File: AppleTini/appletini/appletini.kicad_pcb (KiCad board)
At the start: 2 copper layers, 114.3 x 69.8 mm, 28 parts, among them J1 Conn_02x25_Counter_Clockwise, Q1 DMG2305UX-7, U1 74LS245, U10 74LS07, U16 Pico, U17 Teensy4.1, U2 74LS245, U3 74LS245, U4 74LS245, U9 74LS245

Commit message: part picks and cleanup
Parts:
- R9: value 10k -> 10K

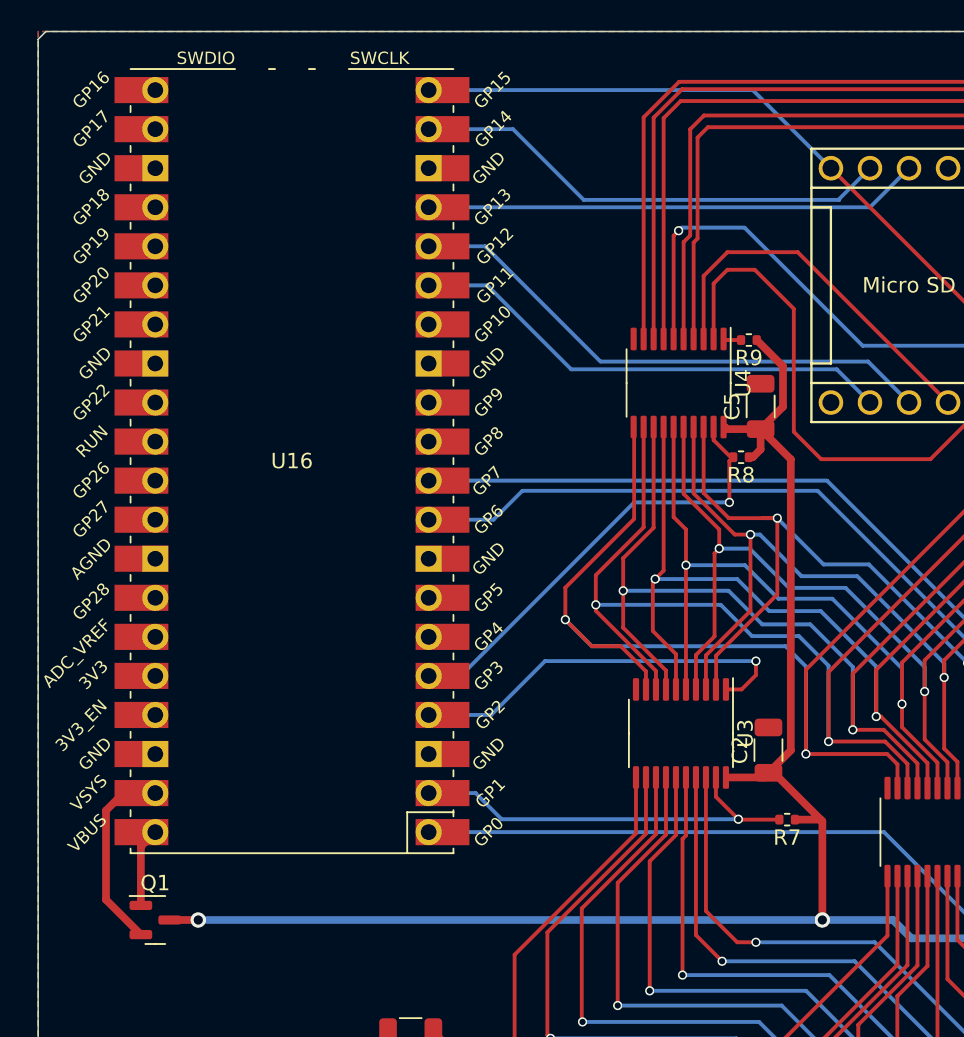
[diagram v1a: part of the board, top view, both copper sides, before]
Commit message: Add pico reset, rotate pico to point USB up
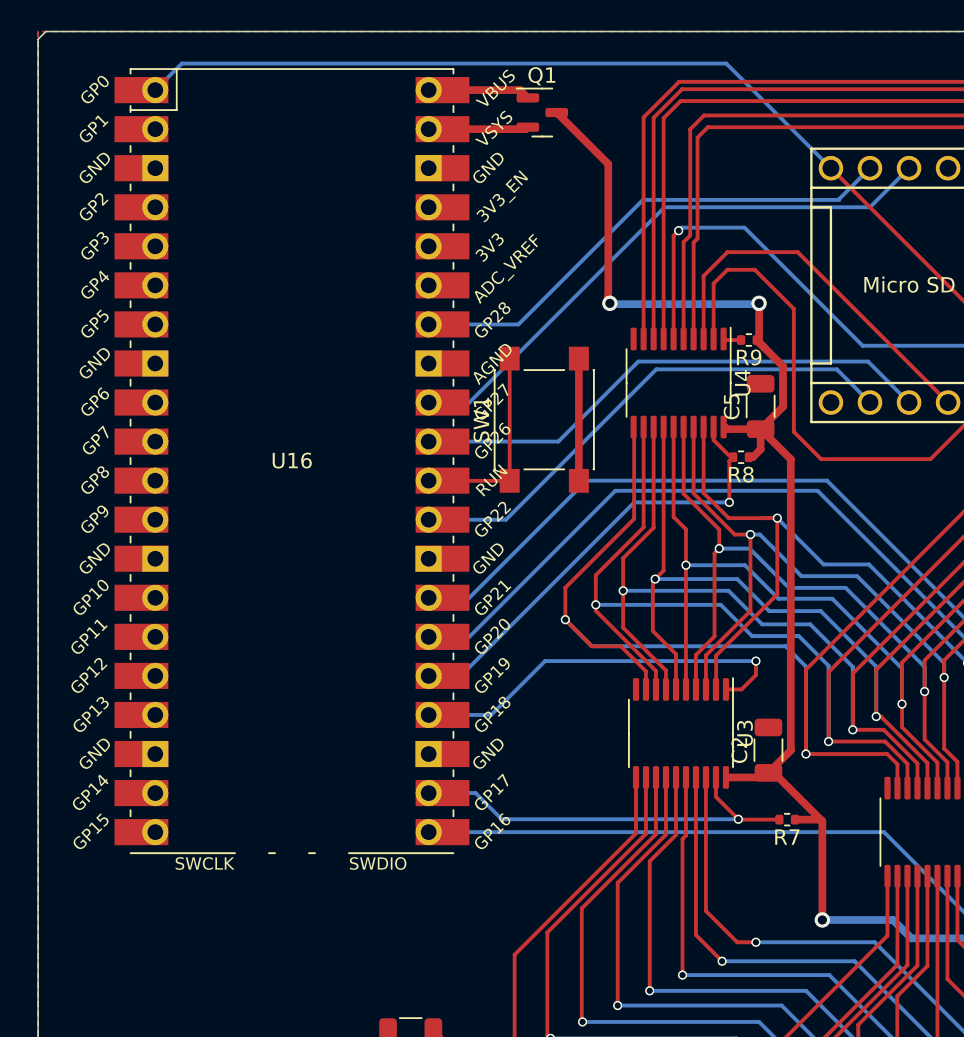
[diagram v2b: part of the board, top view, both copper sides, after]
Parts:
- added SW1: SW_Push, Button_Switch_SMD:SW_Push_1P1T_NO_6x6mm_H9.5mm, F.Cu at (109.1, 88.7)
- moved Q1 58.2 mm to (109.0, 68.8)
- turned U16 to 0 degrees
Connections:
- U16 pad 1: /ALO_EN -> /PHI0
- U16 pad 10: /RDY -> unconnected-(U16-GPIO7-Pad10)
- U16 pad 15: /INH_REQ -> unconnected-(U16-GPIO11-Pad15)
- U16 pad 16: /RDY_REQ -> unconnected-(U16-GPIO12-Pad16)
- U16 pad 17: /TEENSY_IRQ -> unconnected-(U16-GPIO13-Pad17)
- U16 pad 19: /OUT_D_REQ -> unconnected-(U16-GPIO14-Pad19)
- U16 pad 2: /D_EN -> unconnected-(U16-GPIO1-Pad2)
- U16 pad 20: /PHI0 -> unconnected-(U16-GPIO15-Pad20)
- U16 pad 21: unconnected-(U16-GPIO16-Pad21) -> /ALO_EN
- U16 pad 22: unconnected-(U16-GPIO17-Pad22) -> /D_EN
- U16 pad 24: unconnected-(U16-GPIO18-Pad24) -> /D_DIR
- U16 pad 25: unconnected-(U16-GPIO19-Pad25) -> /OUT_D_EN
- U16 pad 26: unconnected-(U16-GPIO20-Pad26) -> /INH
- U16 pad 27: unconnected-(U16-GPIO21-Pad27) -> /RDY
- U16 pad 29: unconnected-(U16-GPIO22-Pad29) -> /INH_REQ
- U16 pad 30: unconnected-(U16-RUN-Pad30) -> Net-(U16-RUN)
- U16 pad 31: unconnected-(U16-GPIO26_ADC0-Pad31) -> /RDY_REQ
- U16 pad 32: unconnected-(U16-GPIO27_ADC1-Pad32) -> /TEENSY_IRQ
- U16 pad 34: unconnected-(U16-GPIO28_ADC2-Pad34) -> /OUT_D_REQ
- U16 pad 4: /D_DIR -> unconnected-(U16-GPIO2-Pad4)
- U16 pad 5: /OUT_D_EN -> unconnected-(U16-GPIO3-Pad5)
- U16 pad 9: /INH -> unconnected-(U16-GPIO6-Pad9)
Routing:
- net /PHI0: track 85.9 -> 105.1 mm
- net +3.3V: track 232.1 -> 216.7 mm, vias 10 -> 11
- net Net-(U16-RUN): track 0.00 -> 13.2 mm
- net GND: track 68.7 -> 76.7 mm
- net /VSYS: track 14.4 -> 6.51 mm
- net /TEENSY_IRQ: track 32.3 -> 37.6 mm
- net unconnected-(U16-GPIO14-Pad19): track 0.00 -> 3.74 mm
- net /RDY: track 94.9 -> 98.0 mm
- net /INH: track 78.7 -> 81.9 mm
- net /INH_REQ: track 31.9 -> 33.6 mm
- net /VBUS: track 5.15 -> 6.66 mm
- net /OUT_D_REQ: track 31.5 -> 32.9 mm
- net /RDY_REQ: track 35.5 -> 34.5 mm

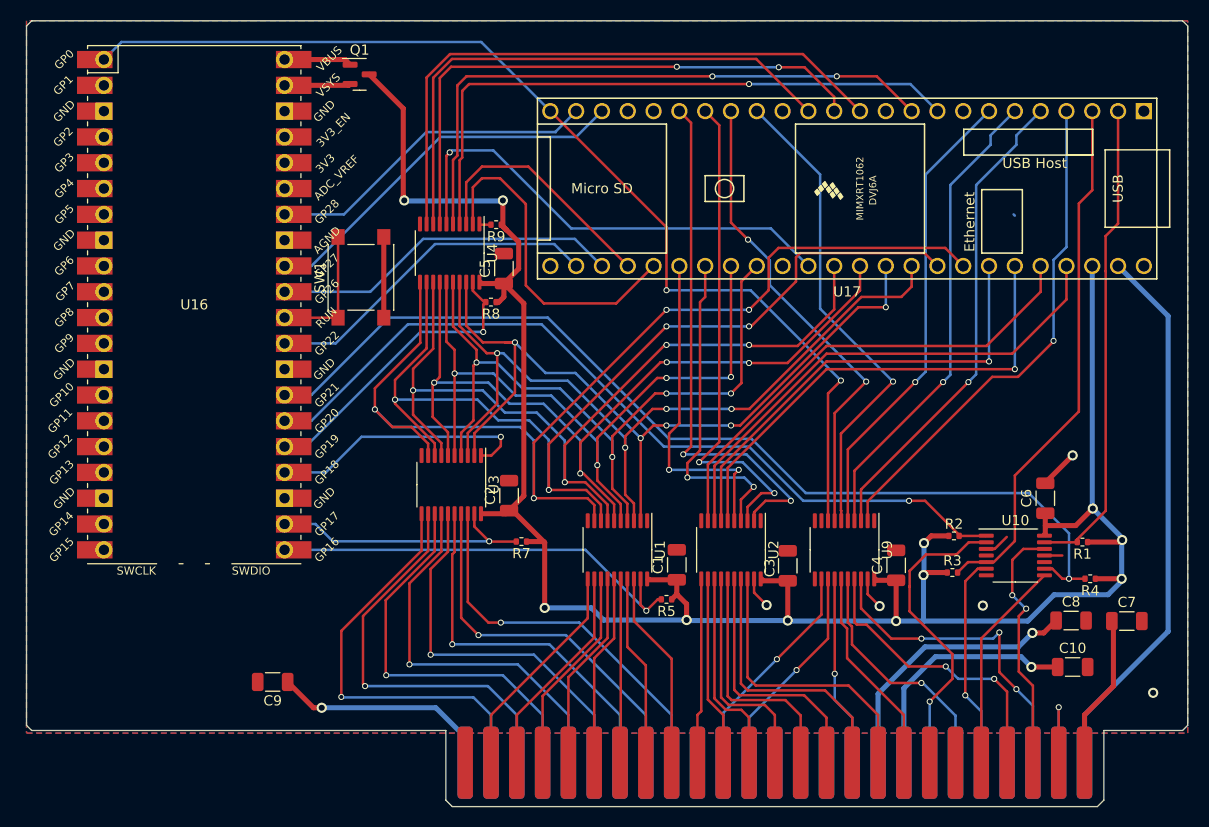
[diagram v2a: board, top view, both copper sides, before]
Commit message: reduce board to 2.625in vertical
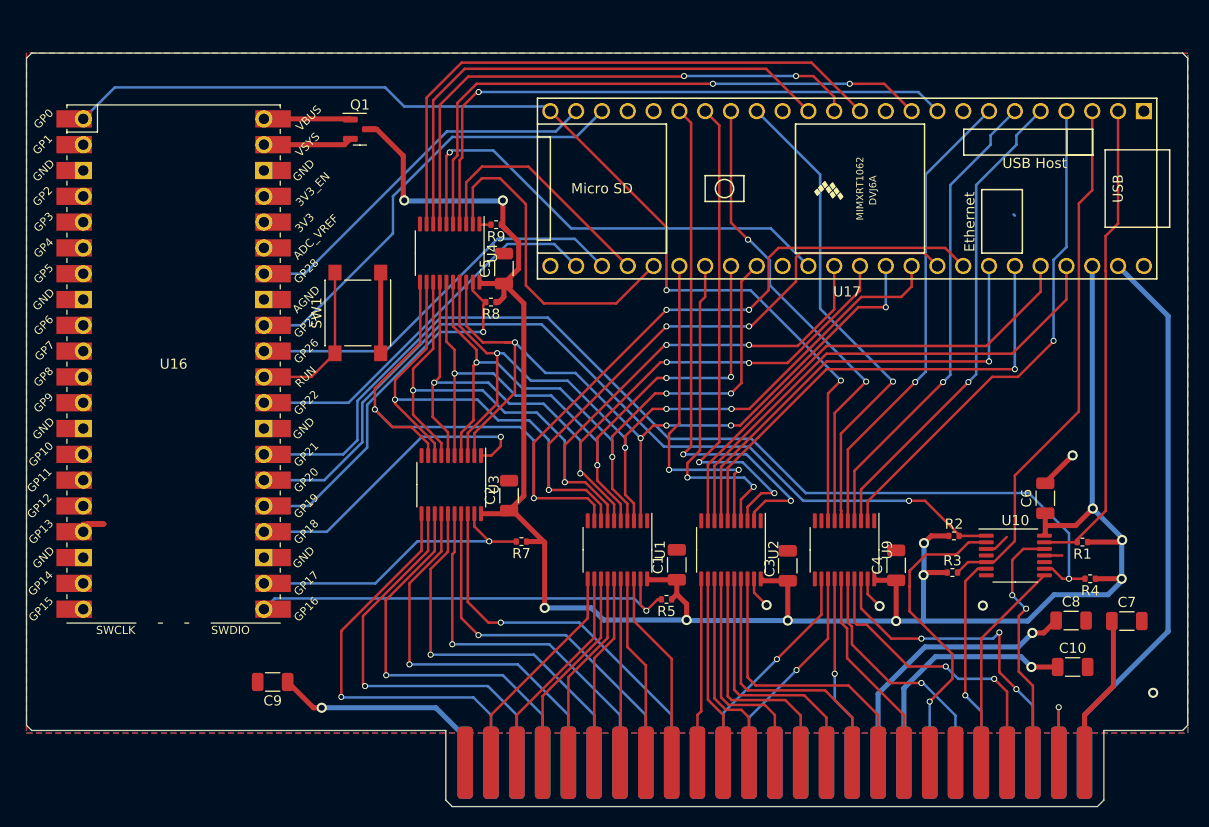
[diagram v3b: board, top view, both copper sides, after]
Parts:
- moved U16 6.19 mm to (90.7, 97.3)
- moved Q1 5.40 mm to (109.0, 74.2)
- moved SW1 3.52 mm to (108.8, 92.3)
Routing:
- net /OUT_D_EN: track 29.9 -> 36.8 mm
- net /RDY: track 98.0 -> 104.8 mm
- net /INH: track 81.9 -> 88.6 mm
- net /TEENSY_IRQ: track 37.6 -> 44.2 mm
- net +3.3V: track 216.7 -> 211.7 mm
- net /D_DIR: track 26.0 -> 30.4 mm
- net /RDY_REQ: track 34.5 -> 39.0 mm
- net /INH_REQ: track 33.6 -> 38.1 mm
- net /OUT_D_REQ: track 32.9 -> 37.4 mm
- net unconnected-(U16-GPIO14-Pad19): track 3.74 -> 0.00 mm
- net unconnected-(U16-GPIO13-Pad17): track 0.00 -> 3.74 mm
- net /D_EN: track 26.8 -> 29.9 mm
- net Net-(U16-RUN): track 13.2 -> 15.9 mm
- net /Transceivers/OUT_D2: track 56.3 -> 54.0 mm
- net /VSYS: track 6.51 -> 8.75 mm
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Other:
- board size 114.3 x 69.8 mm -> 114.3 x 66.7 mm

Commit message: traces wiped
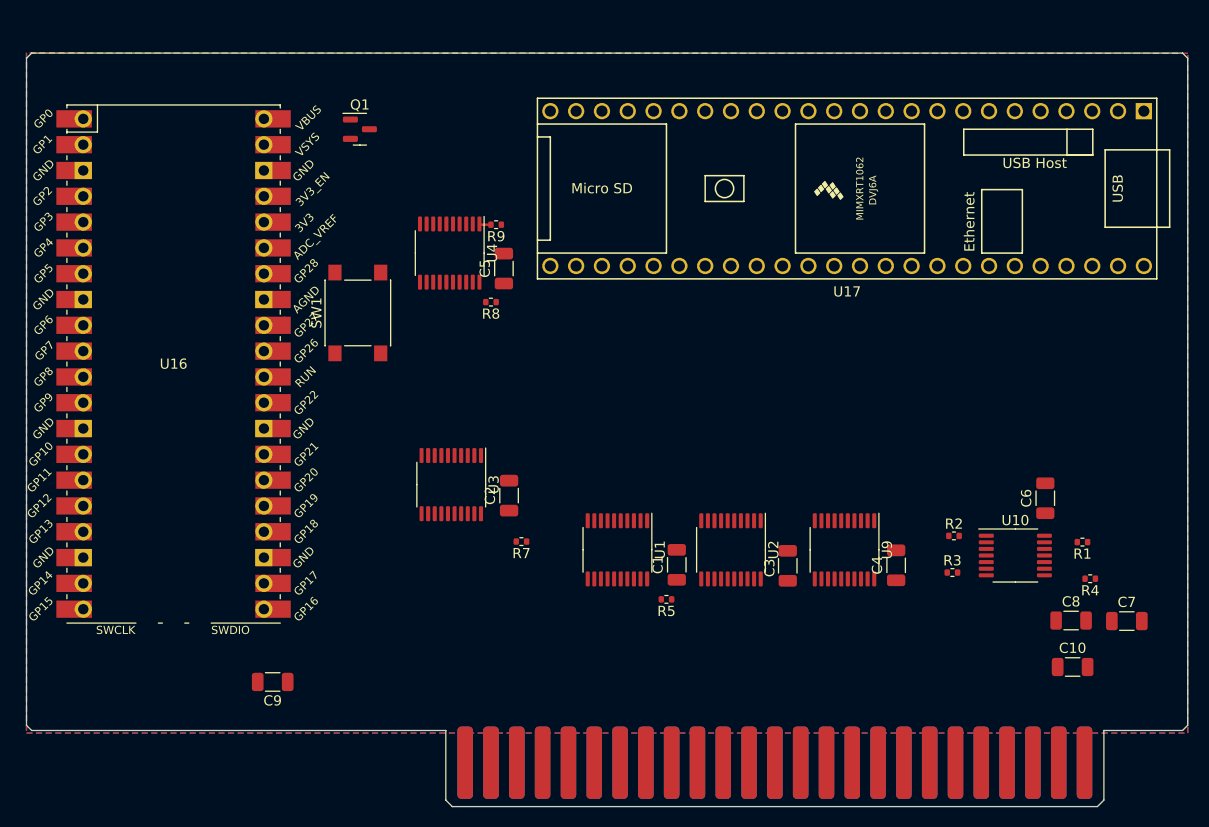
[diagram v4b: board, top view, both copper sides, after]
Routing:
- net +3.3V: track 211.7 -> 0.00 mm, vias 11 -> 0
- net /Transceivers/ALO_D0: track 110.9 -> 0.00 mm, vias 4 -> 0
- net /PHI0: track 105.8 -> 0.00 mm, vias 2 -> 0
- net /RDY: track 104.8 -> 0.00 mm, vias 1 -> 0
- net /Transceivers/ALO_D1: track 101.5 -> 0.00 mm, vias 4 -> 0
- net /INH: track 88.6 -> 0.00 mm, vias 1 -> 0
- net /Transceivers/ALO_D2: track 86.9 -> 0.00 mm, vias 4 -> 0
- net /Transceivers/ALO_D3: track 83.4 -> 0.00 mm, vias 4 -> 0
- net /Transceivers/ALO_D6: track 82.4 -> 0.00 mm, vias 4 -> 0
- net /Transceivers/ALO_D7: track 81.5 -> 0.00 mm, vias 5 -> 0
- net GND: track 76.7 -> 0.00 mm, vias 5 -> 0
- net /Transceivers/ALO_D5: track 72.8 -> 0.00 mm, vias 4 -> 0
- net /Transceivers/ALO_D4: track 72.2 -> 0.00 mm, vias 4 -> 0
- net /Transceivers/OUT_D5: track 59.8 -> 0.00 mm, vias 1 -> 0
- net /Transceivers/OUT_D4: track 58.7 -> 0.00 mm, vias 2 -> 0
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
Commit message: 4 layer complete
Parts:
- added JP1: Jumper_2_Open, Connector_PinHeader_2.54mm:PinHeader_1x02_P2.54mm_Vertical, F.Cu at (183.9, 93.2)
- moved C10 17.4 mm to (161.7, 127.9), turned to 180 degrees
- moved C8 17.3 mm to (161.7, 122.7)
- moved C9 14.6 mm to (114.9, 130.0)
- moved U9 9.11 mm to (161.6, 107.9)
- moved C4 9.11 mm to (166.7, 109.4)
- moved R1 5.85 mm to (185.9, 113.9)
- moved C6 5.85 mm to (182.3, 109.5)
- moved U10 5.85 mm to (179.3, 115.2)
- moved R3 5.81 mm to (173.0, 116.4)
- moved R4 5.59 mm to (175.6, 120.2), turned to 0 degrees
- moved R2 5.42 mm to (172.7, 112.8)
- moved C7 4.34 mm to (185.9, 126.7)
- moved R5 1.59 mm to (138.5, 121.9)
- moved R9 1.44 mm to (122.6, 82.1)
- moved R7 1.39 mm to (123.5, 114.6)
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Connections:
- net /BUS_DMAIN renamed /BUS_DMAPASS
- Q1 pad 3: +3.3V -> +5V
- U17 pad 48: unconnected-(U17-VIN-Pad48) -> /VIN
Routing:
- net +5V: track 0.00 -> 154.2 mm, vias 0 -> 1
- net /PHI0: track 0.00 -> 126.9 mm
- net /Transceivers/ALO_D0: track 0.00 -> 96.7 mm, vias 0 -> 2
- net /Transceivers/ALO_D1: track 0.00 -> 92.9 mm, vias 0 -> 2
- net /RDY: track 0.00 -> 92.3 mm, vias 0 -> 1
- net /Transceivers/ALO_D7: track 0.00 -> 91.5 mm, vias 0 -> 2
- net /Transceivers/ALO_D2: track 0.00 -> 89.3 mm, vias 0 -> 2
- net /INH: track 0.00 -> 88.8 mm, vias 0 -> 1
- net /Transceivers/ALO_D6: track 0.00 -> 83.3 mm, vias 0 -> 2
- net /Transceivers/ALO_D3: track 0.00 -> 81.0 mm, vias 0 -> 2
- net /Transceivers/OUT_D1: track 0.00 -> 73.5 mm
- net /Transceivers/ALO_D5: track 0.00 -> 69.3 mm, vias 0 -> 2
- net /Transceivers/ALO_D4: track 0.00 -> 66.9 mm, vias 0 -> 2
- net /Transceivers/OUT_D4: track 0.00 -> 65.6 mm, vias 0 -> 1
- net /M2B0: track 0.00 -> 56.5 mm
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- added copper zone on In2.Cu, net +3.3V
- added copper zone on In1.Cu, net GND
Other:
- copper layers 2 -> 4

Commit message: revisions, passed JLCPCB verification
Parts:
- removed U10: 74LS07, Package_SO:TSSOP-14_4.4x5mm_P0.65mm
- added U6: 74LS07, Package_SO:TSSOP-14_4.4x5mm_P0.65mm, F.Cu at (179.2, 115.2)
- renumbered R7 to R6, R8 to R7, R9 to R8, U9 to U5, U16 to U7, U17 to U8
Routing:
- net /INH: track 88.8 -> 89.9 mm
- net /D_DIR: vias 0 -> 1

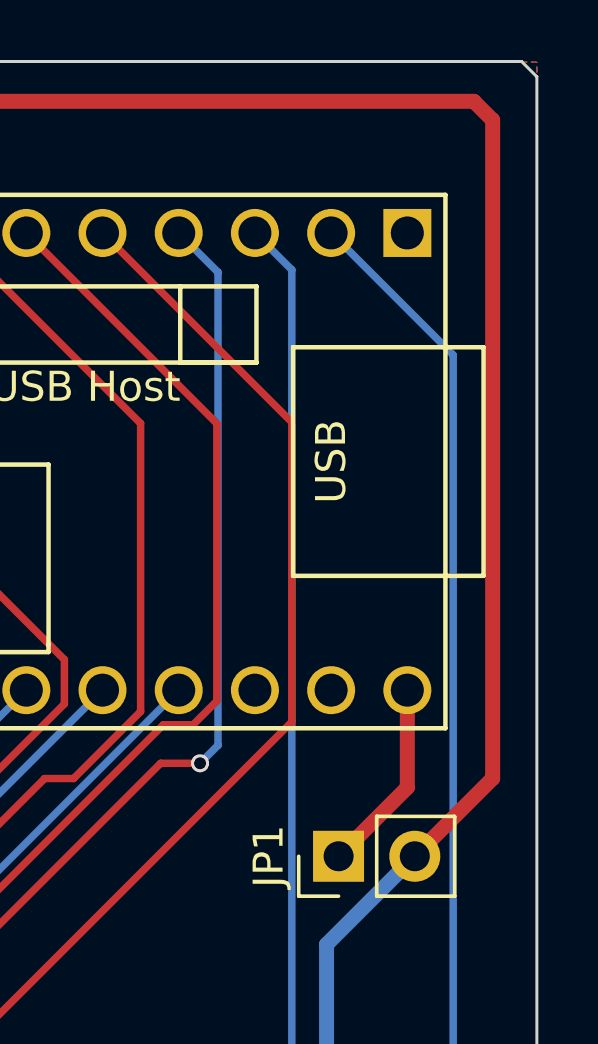
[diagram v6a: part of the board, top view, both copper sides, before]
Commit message: change Pico power from 5v to VIN
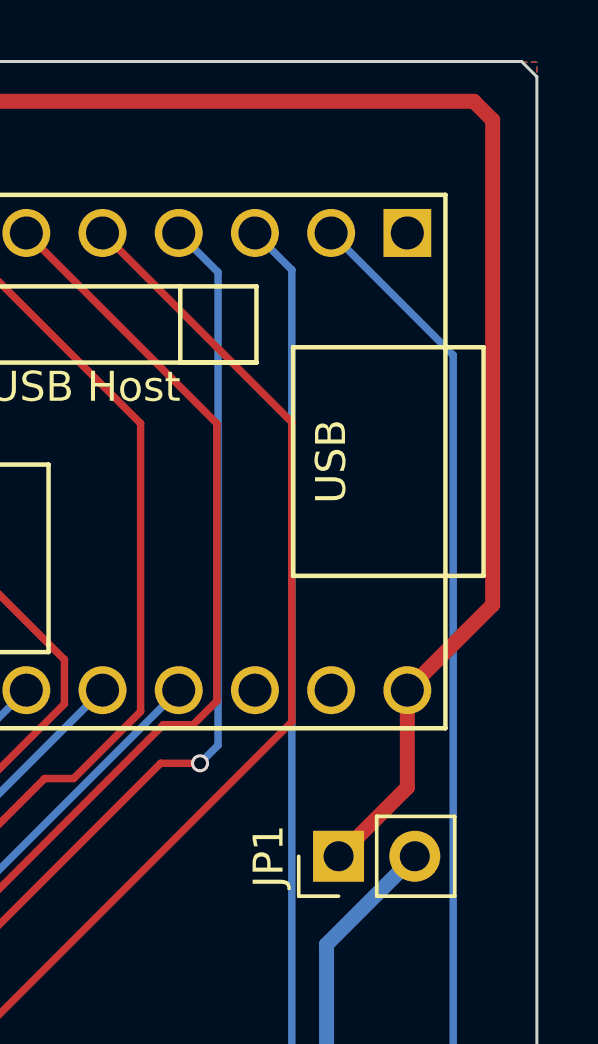
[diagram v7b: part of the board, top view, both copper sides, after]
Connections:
- Q1 pad 3: +5V -> /VIN
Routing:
- net +5V: track 154.2 -> 46.7 mm
- net /VIN: track 6.49 -> 108.6 mm
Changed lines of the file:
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@@
       (net 50 "/VSYS") (pinfunction "S") (pintype "passive"))
     (pad "3" smd roundrect (at 0.9375 0) (size 1.475 0.6) (layers "F.Cu" "F.Paste" "F.Mask") (roundrect_rratio 0.25)
-      (net 31 "+5V") (pinfunction "D") (pintype "passive"))
+      (net 97 "/VIN") (pinfunction "D") (pintype "passive"))
     (model "${KICAD6_3DMODEL_DIR}/Package_TO_SOT_SMD.3dshapes/SOT-23.wrl"
       (offset (xyz 0 0 0))
@@
   (segment (start 169.5196 125.3744) (end 165.1 129.794) (width 0.25) (layer "B.Cu") (net 30))
   (segment (start 169.5196 122.0724) (end 169.5196 125.3744) (width 0.25) (layer "B.Cu") (net 30))
-  (segment (start 109.9543 74.168) (end 116.1205 68.0018) (width 0.5) (layer "F.Cu") (net 31))
   (segment (start 180.34 136.525) (end 180.34 130.7574) (width 0.5) (layer "F.Cu") (net 31))
-  (segment (start 116.1205 68.0018) (end 188.3978 68.0018) (width 0.5) (layer "F.Cu") (net 31))
   (segment (start 184.4022 124.3094) (end 184.404 124.2568) (width 0.5) (layer "F.Cu") (net 31))
-  (segment (start 189.0268 68.6308) (end 189.0268 90.5714) (width 0.5) (layer "F.Cu") (net 31))
   (segment (start 184.404 124.2568) (end 184.4022 126.6952) (width 0.5) (layer "F.Cu") (net 31))
-  (segment (start 188.3978 68.0018) (end 189.0268 68.6308) (width 0.5) (layer "F.Cu") (net 31))
-  (segment (start 189.0268 90.5714) (end 186.431 93.1672) (width 0.5) (layer "F.Cu") (net 31))
   (segment (start 180.34 130.7574) (end 184.4022 126.6952) (width 0.5) (layer "F.Cu") (net 31))
   (via (at 184.404 124.2568) (size 1) (drill 0.6) (layers "F.Cu" "B.Cu") (net 31))
@@
   (segment (start 99.568 98.552) (end 104.2394 98.552) (width 0.25) (layer "F.Cu") (net 80))
   (segment (start 104.2394 98.552) (end 106.5636 96.2278) (width 0.25) (layer "F.Cu") (net 80))
+  (segment (start 116.1205 68.0018) (end 188.3978 68.0018) (width 0.5) (layer "F.Cu") (net 97))
   (segment (start 186.182 90.8762) (end 186.182 87.63) (width 0.5) (layer "F.Cu") (net 97))
+  (segment (start 189.0268 84.7852) (end 186.182 87.63) (width 0.5) (layer "F.Cu") (net 97))
+  (segment (start 188.3978 68.0018) (end 189.0268 68.6308) (width 0.5) (layer "F.Cu") (net 97))
+  (segment (start 189.0268 68.6308) (end 189.0268 84.7852) (width 0.5) (layer "F.Cu") (net 97))
   (segment (start 183.891 93.1672) (end 186.182 90.8762) (width 0.5) (layer "F.Cu") (net 97))
+  (segment (start 109.9543 74.168) (end 116.1205 68.0018) (width 0.5) (layer "F.Cu") (net 97))
   (segment (start 120.131 82.768513) (end 120.131 83.4975) (width 0.25) (layer "F.Cu") (net 98))
   (segment (start 131.5212 81.2292) (end 121.670313 81.2292) (width 0.25) (layer "F.Cu") (net 98))
